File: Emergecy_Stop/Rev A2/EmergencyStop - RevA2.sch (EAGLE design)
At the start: 12 parts, among them J1 MSTBA2, J2 MSTBA3, J3 NC3FBV2-SW, J4 NC3MAV, T1 EXMACHINA-LOGO-NAME

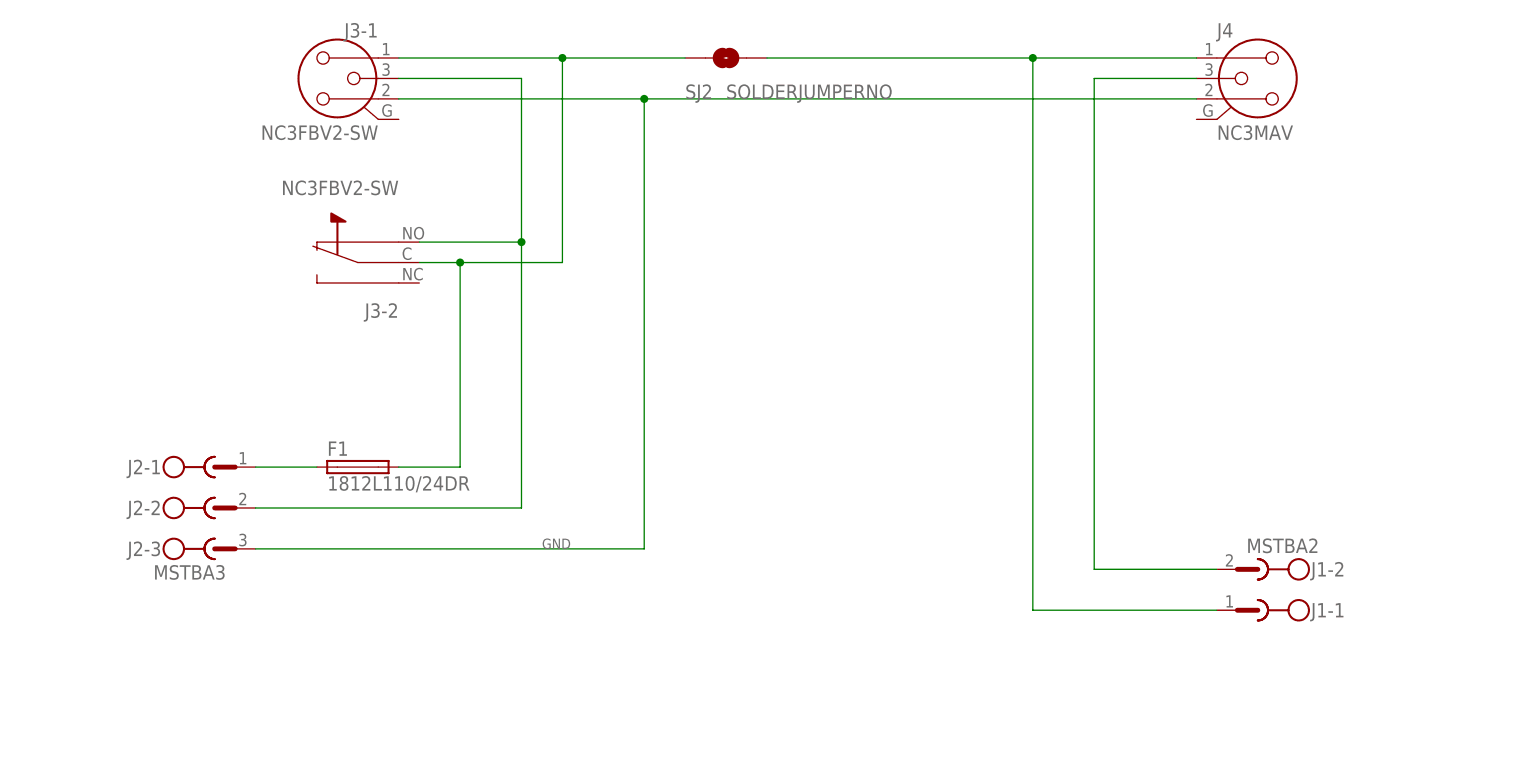
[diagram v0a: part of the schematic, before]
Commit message: Replace MSTBA with Molex headers and reroute
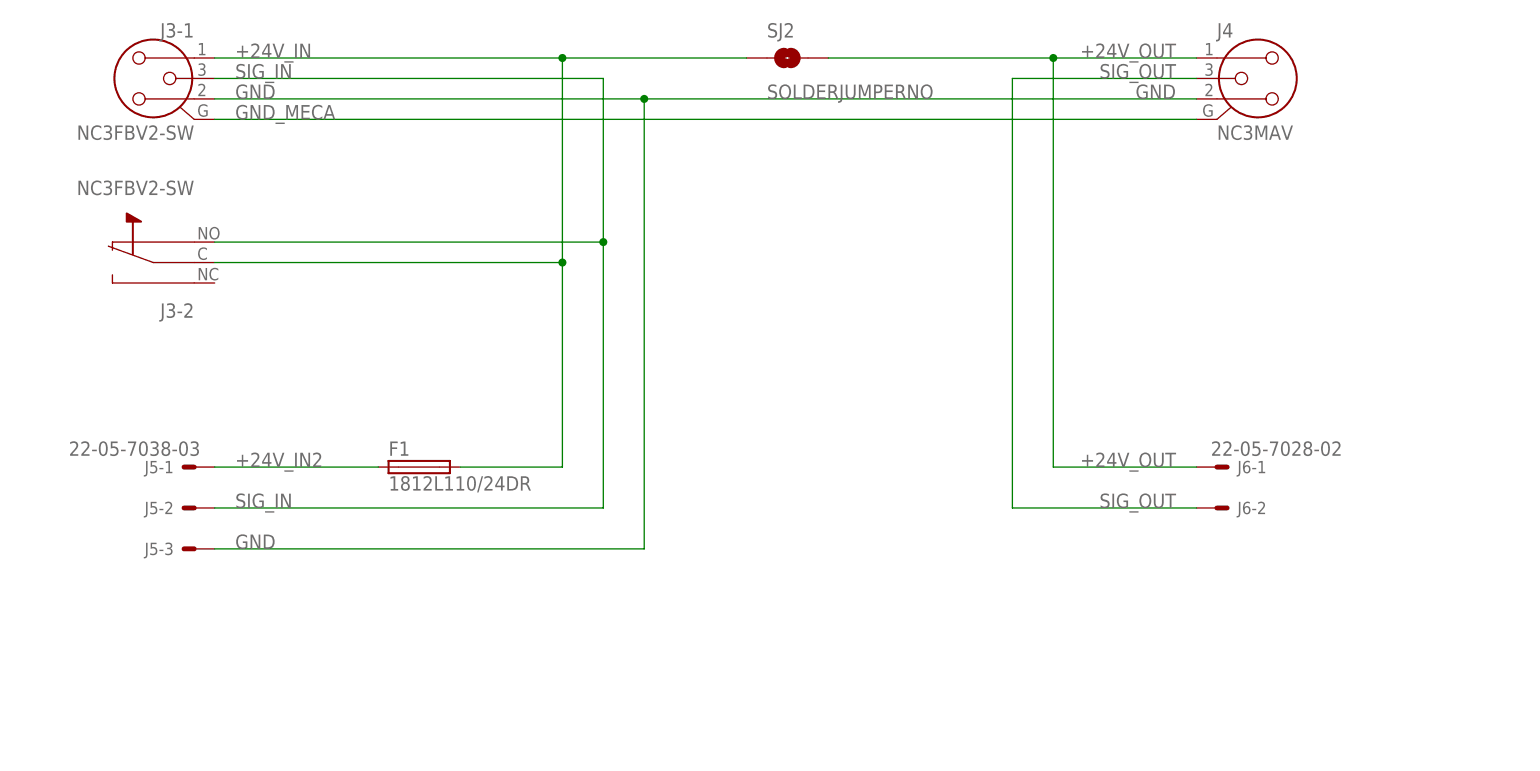
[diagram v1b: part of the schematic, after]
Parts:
- removed J1: MSTBA2, con-phoenix-508:MSTBA2
- removed J2: MSTBA3, con-phoenix-508:MSTBA3
- added J5: 22-05-7038-03, con-molex:22-05-7038-03
- added J6: 22-05-7028-02, con-molex:22-05-7028-02
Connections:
- removed net N$1: F1.1, J2-1.1
- new net +24V_IN2: F1.1, J5-1.S
- new net GND_MECA: J3-1.G, J4.G
- net +24V_OUT: now also J6-1.S; no longer J1-1.1
- net GND: now also J5-3.S; no longer J2-3.1
- net SIG_IN: now also J5-2.S; no longer J2-2.1
- net SIG_OUT: now also J6-2.S; no longer J1-2.1
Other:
- moved on the sheet: F1, J3-1, J3-2, SJ2
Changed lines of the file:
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@@
 </variantdefs>
 <classes>
-<class number="0" name="default" width="0" drill="0">
+<class number="0" name="default" width="0.8128" drill="0.35">
 </class>
 </classes>
 <parts>
 <part name="FRAME1" library="frames" deviceset="A3L-LOC" device=""/>
-<part name="J2" library="con-phoenix-508" deviceset="MSTBA3" device=""/>
 <part name="J4" library="con-neutrik_ag" deviceset="NC3" device="MAV"/>
-<part name="J1" library="con-phoenix-508" deviceset="MSTBA2" device=""/>
 <part name="J3" library="con-neutrik_ag" deviceset="NC3?-SW" device="FBV2"/>
 <part name="SJ2" library="SparkFun-Passives" deviceset="SOLDERJUMPER" device="NO"/>
@@
 <part name="JP3" library="SparkFun" deviceset="FIDUCIAL" device="1X2"/>
 <part name="JP4" library="SparkFun" deviceset="FIDUCIAL" device="1X2"/>
+<part name="J5" library="con-molex" deviceset="22-?-03" device="05-7038"/>
+<part name="J6" library="con-molex" deviceset="22-?-02" device="05-7028"/>
 </parts>
 <sheets>
@@
 <instances>
 <instance part="FRAME1" gate="G$1" x="0" y="0"/>
-<instance part="J2" gate="-1" x="104.14" y="139.7"/>
-<instance part="J2" gate="-2" x="104.14" y="134.62"/>
-<instance part="J2" gate="-3" x="104.14" y="129.54"/>
 <instance part="J4" gate="G$1" x="233.68" y="187.96"/>
-<instance part="J1" gate="-1" x="233.68" y="121.92" rot="R180"/>
-<instance part="J1" gate="-2" x="233.68" y="127" rot="R180"/>
-<instance part="J3" gate="-1" x="119.38" y="187.96" rot="MR0"/>
-<instance part="J3" gate="-2" x="121.92" y="165.1" rot="R180"/>
-<instance part="SJ2" gate="1" x="167.64" y="190.5" smashed="yes">
-<attribute name="NAME" x="162.56" y="185.42" size="1.778" layer="95"/>
-<attribute name="VALUE" x="167.64" y="185.42" size="1.778" layer="96"/>
-</instance>
-<instance part="F1" gate="G$1" x="121.92" y="139.7"/>
+<instance part="J3" gate="-1" x="96.52" y="187.96" rot="MR0"/>
+<instance part="J3" gate="-2" x="96.52" y="165.1" rot="R180"/>
+<instance part="SJ2" gate="1" x="175.26" y="190.5"/>
+<instance part="F1" gate="G$1" x="129.54" y="139.7"/>
 <instance part="CC1" gate="G$1" x="303.53" y="8.89"/>
 <instance part="T1" gate="G$1" x="311.15" y="19.05"/>
@@
 <instance part="JP3" gate="G$1" x="352.806" y="21.844"/>
 <instance part="JP4" gate="G$1" x="356.87" y="21.844"/>
+<instance part="J5" gate="-1" x="101.6" y="139.7" rot="MR0"/>
+<instance part="J5" gate="-2" x="101.6" y="134.62" rot="MR0"/>
+<instance part="J5" gate="-3" x="101.6" y="129.54" rot="MR0"/>
+<instance part="J6" gate="-1" x="228.6" y="139.7"/>
+<instance part="J6" gate="-2" x="228.6" y="134.62"/>
 </instances>
 <busses>
@@
 <segment>
 <pinref part="F1" gate="G$1" pin="2"/>
-<wire x1="127" y1="139.7" x2="134.62" y2="139.7" width="0.1524" layer="91"/>
+<wire x1="134.62" y1="139.7" x2="147.32" y2="139.7" width="0.1524" layer="91"/>
 <pinref part="J3" gate="-1" pin="1"/>
 <pinref part="SJ2" gate="1" pin="1"/>
-<wire x1="127" y1="190.5" x2="147.32" y2="190.5" width="0.1524" layer="91"/>
 <pinref part="J3" gate="-2" pin="N"/>
-<wire x1="147.32" y1="190.5" x2="162.56" y2="190.5" width="0.1524" layer="91"/>
-<wire x1="129.54" y1="165.1" x2="134.62" y2="165.1" width="0.1524" layer="91"/>
-<wire x1="134.62" y1="165.1" x2="147.32" y2="165.1" width="0.1524" layer="91"/>
+<wire x1="104.14" y1="190.5" x2="147.32" y2="190.5" width="0.1524" layer="91"/>
+<wire x1="147.32" y1="190.5" x2="170.18" y2="190.5" width="0.1524" layer="91"/>
+<wire x1="104.14" y1="165.1" x2="147.32" y2="165.1" width="0.1524" layer="91"/>
 <wire x1="147.32" y1="165.1" x2="147.32" y2="190.5" width="0.1524" layer="91"/>
 <junction x="147.32" y="190.5"/>
-<wire x1="134.62" y1="139.7" x2="134.62" y2="165.1" width="0.1524" layer="91"/>
-<junction x="134.62" y="165.1"/>
+<wire x1="147.32" y1="139.7" x2="147.32" y2="165.1" width="0.1524" layer="91"/>
+<junction x="147.32" y="165.1"/>
+<label x="106.68" y="190.5" size="1.778" layer="95"/>
 </segment>
 </net>
 <net name="SIG_IN" class="0">
 <segment>
-<pinref part="J2" gate="-2" pin="1"/>
-<wire x1="109.22" y1="134.62" x2="142.24" y2="134.62" width="0.1524" layer="91"/>
 <pinref part="J3" gate="-1" pin="3"/>
-<wire x1="127" y1="187.96" x2="142.24" y2="187.96" width="0.1524" layer="91"/>
-<wire x1="142.24" y1="187.96" x2="142.24" y2="167.64" width="0.1524" layer="91"/>
+<wire x1="104.14" y1="134.62" x2="152.4" y2="134.62" width="0.1524" layer="91"/>
+<wire x1="104.14" y1="187.96" x2="152.4" y2="187.96" width="0.1524" layer="91"/>
+<wire x1="152.4" y1="187.96" x2="152.4" y2="167.64" width="0.1524" layer="91"/>
 <pinref part="J3" gate="-2" pin="NO"/>
-<wire x1="142.24" y1="167.64" x2="129.54" y2="167.64" width="0.1524" layer="91"/>
-<wire x1="142.24" y1="167.64" x2="142.24" y2="134.62" width="0.1524" layer="91"/>
-<junction x="142.24" y="167.64"/>
+<wire x1="152.4" y1="167.64" x2="104.14" y2="167.64" width="0.1524" layer="91"/>
+<wire x1="152.4" y1="167.64" x2="152.4" y2="134.62" width="0.1524" layer="91"/>
+<junction x="152.4" y="167.64"/>
+<pinref part="J5" gate="-2" pin="S"/>
+<label x="106.68" y="134.62" size="1.778" layer="95"/>
+<label x="106.68" y="187.96" size="1.778" layer="95"/>
 </segment>
 </net>
 <net name="+24V_OUT" class="0">
 <segment>
-<pinref part="J1" gate="-1" pin="1"/>
-<wire x1="228.6" y1="121.92" x2="205.74" y2="121.92" width="0.1524" layer="91"/>
-<wire x1="205.74" y1="121.92" x2="205.74" y2="190.5" width="0.1524" layer="91"/>
 <pinref part="SJ2" gate="1" pin="2"/>
 <pinref part="J4" gate="G$1" pin="1"/>
-<wire x1="172.72" y1="190.5" x2="205.74" y2="190.5" width="0.1524" layer="91"/>
-<wire x1="205.74" y1="190.5" x2="226.06" y2="190.5" width="0.1524" layer="91"/>
-<junction x="205.74" y="190.5"/>
+<wire x1="208.28" y1="139.7" x2="208.28" y2="190.5" width="0.1524" layer="91"/>
+<wire x1="180.34" y1="190.5" x2="208.28" y2="190.5" width="0.1524" layer="91"/>
+<wire x1="208.28" y1="190.5" x2="226.06" y2="190.5" width="0.1524" layer="91"/>
+<junction x="208.28" y="190.5"/>
+<pinref part="J6" gate="-1" pin="S"/>
+<wire x1="226.06" y1="139.7" x2="208.28" y2="139.7" width="0.1524" layer="91"/>
+<label x="223.52" y="139.7" size="1.778" layer="95" rot="MR0"/>
+<label x="223.52" y="190.5" size="1.778" layer="95" rot="MR0"/>
 </segment>
 </net>
-<net name="N$1" class="0">
+<net name="+24V_IN2" class="0">
 <segment>
-<pinref part="J2" gate="-1" pin="1"/>
 <pinref part="F1" gate="G$1" pin="1"/>
-<wire x1="109.22" y1="139.7" x2="116.84" y2="139.7" width="0.1524" layer="91"/>
+<pinref part="J5" gate="-1" pin="S"/>
+<wire x1="124.46" y1="139.7" x2="104.14" y2="139.7" width="0.1524" layer="91"/>
+<label x="106.68" y="139.7" size="1.778" layer="95"/>
 </segment>
 </net>
 <net name="GND" class="0">
 <segment>
-<pinref part="J2" gate="-3" pin="1"/>
-<wire x1="157.48" y1="129.54" x2="109.22" y2="129.54" width="0.1524" layer="91"/>
+<wire x1="157.48" y1="129.54" x2="104.14" y2="129.54" width="0.1524" layer="91"/>
 <pinref part="J3" gate="-1" pin="2"/>
 <pinref part="J4" gate="G$1" pin="2"/>
-<wire x1="127" y1="185.42" x2="157.48" y2="185.42" width="0.1524" layer="91"/>
+<wire x1="104.14" y1="185.42" x2="157.48" y2="185.42" width="0.1524" layer="91"/>
 <wire x1="157.48" y1="185.42" x2="226.06" y2="185.42" width="0.1524" layer="91"/>
 <wire x1="157.48" y1="129.54" x2="157.48" y2="185.42" width="0.1524" layer="91"/>
 <junction x="157.48" y="185.42"/>
-<label x="144.78" y="129.54" size="1.27" layer="95"/>
+<pinref part="J5" gate="-3" pin="S"/>
+<label x="106.68" y="129.54" size="1.778" layer="95"/>
+<label x="223.52" y="185.42" size="1.778" layer="95" rot="MR0"/>
+<label x="106.68" y="185.42" size="1.778" layer="95"/>
 </segment>
 </net>
 <net name="SIG_OUT" class="0">
 <segment>
-<pinref part="J1" gate="-2" pin="1"/>
-<wire x1="228.6" y1="127" x2="213.36" y2="127" width="0.1524" layer="91"/>
-<wire x1="213.36" y1="127" x2="213.36" y2="187.96" width="0.1524" layer="91"/>
 <pinref part="J4" gate="G$1" pin="3"/>
-<wire x1="213.36" y1="187.96" x2="226.06" y2="187.96" width="0.1524" layer="91"/>
+<wire x1="203.2" y1="134.62" x2="203.2" y2="187.96" width="0.1524" layer="91"/>
+<wire x1="203.2" y1="187.96" x2="226.06" y2="187.96" width="0.1524" layer="91"/>
+<pinref part="J6" gate="-2" pin="S"/>
+<wire x1="226.06" y1="134.62" x2="203.2" y2="134.62" width="0.1524" layer="91"/>
+<label x="223.52" y="134.62" size="1.778" layer="95" rot="MR0"/>
+<label x="223.52" y="187.96" size="1.778" layer="95" rot="MR0"/>
 </segment>
 </net>
+<net name="GND_MECA" class="0">
+<segment>
+<pinref part="J3" gate="-1" pin="G"/>
+<pinref part="J4" gate="G$1" pin="G"/>
+<wire x1="104.14" y1="182.88" x2="226.06" y2="182.88" width="0.1524" layer="91"/>
+<label x="106.68" y="182.88" size="1.778" layer="95"/>
+</segment>
+</net>
